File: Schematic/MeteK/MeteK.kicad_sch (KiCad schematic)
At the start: 6 parts, among them U1 Pico, U2 LM7805_TO220

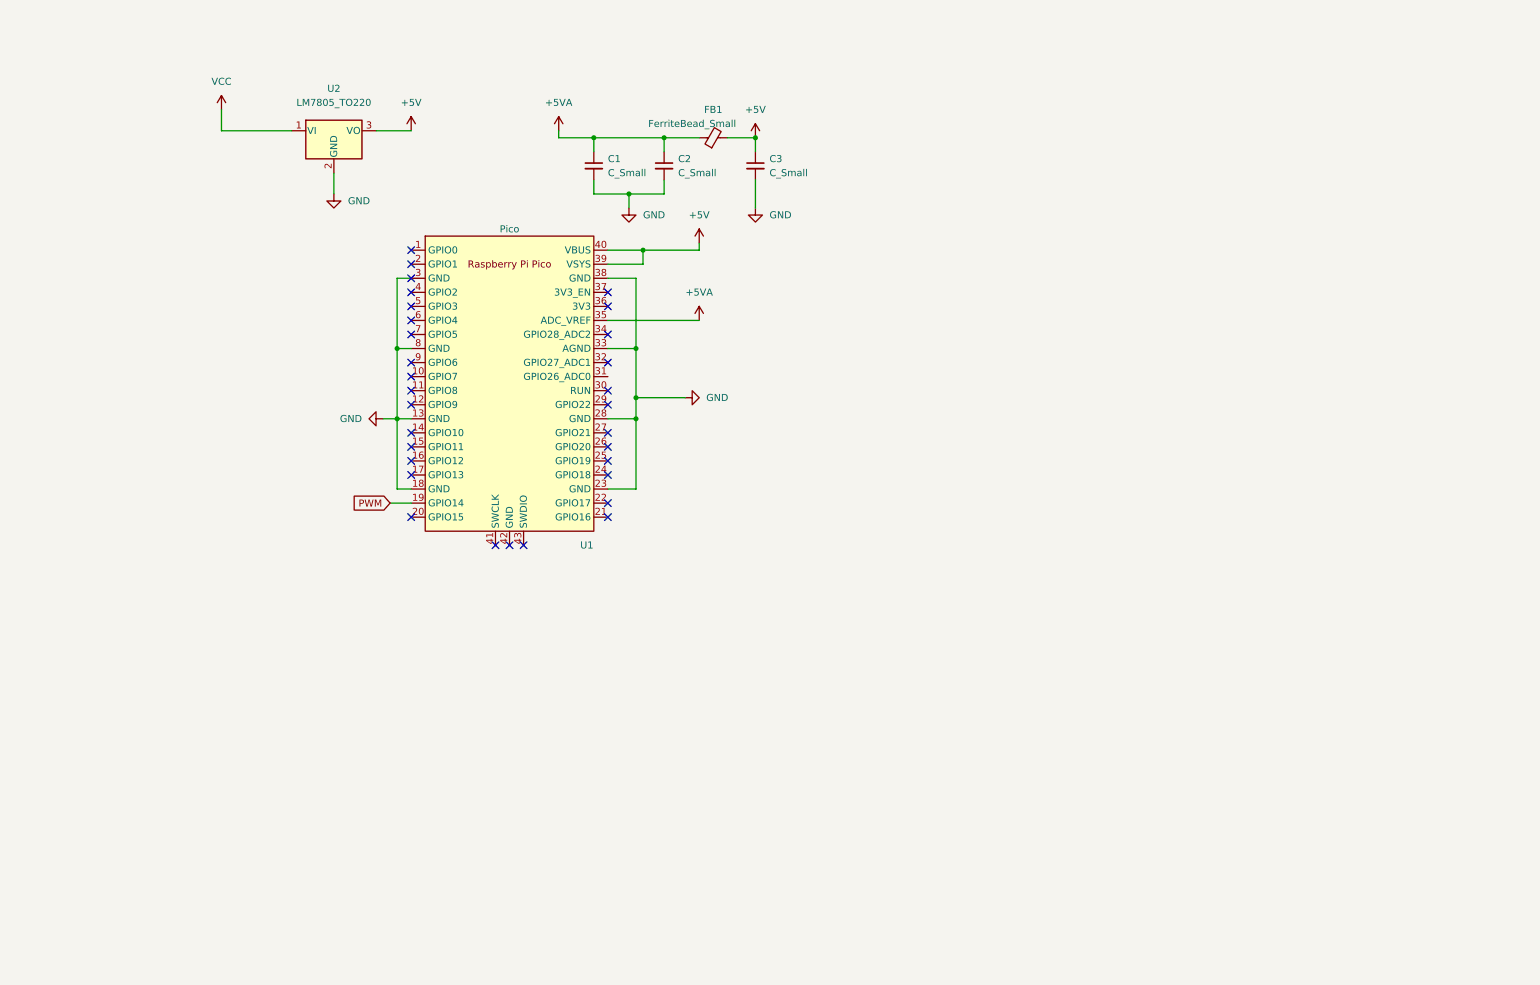
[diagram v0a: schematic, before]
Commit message: Gate driver fixes. Initial KiCad schematic and PCB design trials. Updates on components.
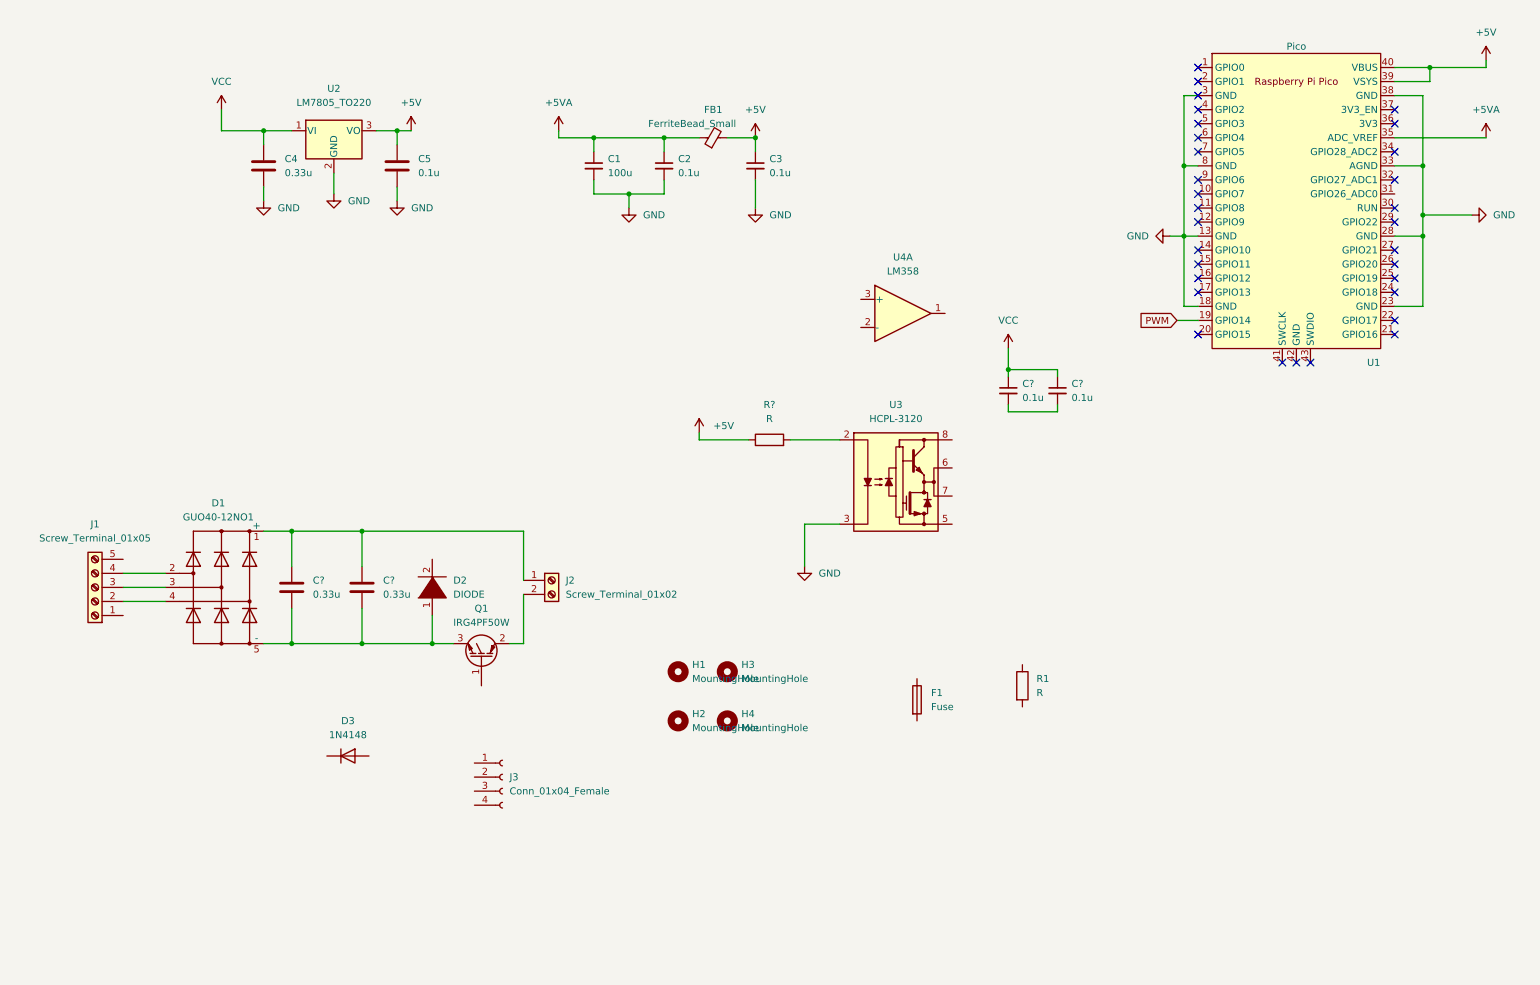
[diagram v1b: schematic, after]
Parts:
- added C4, C? (x2): 0.33u, Capacitor_THT:C_Disc_D3.4mm_W2.1mm_P2.50mm, symbol Device:C
- added C5: 0.1u, Capacitor_THT:C_Disc_D5.0mm_W2.5mm_P2.50mm, symbol Device:C
- added C? (x2): 0.1u, Capacitor_THT:C_Disc_D14.5mm_W5.0mm_P10.00mm, symbol Device:C_Small
- added D1: GUO40-12NO1, Diode_THT:Diode_Bridge_IXYS_GUFP, symbol Diode_Bridge:GUO40-12NO1
- added D2: DIODE, Package_TO_SOT_THT:TO-220-2_Horizontal_TabUp, symbol pspice:DIODE
- added D3: 1N4148, Diode_THT:D_DO-35_SOD27_P7.62mm_Horizontal, symbol Diode:1N4148
- added F1: Fuse, Fuse:Fuse_Bourns_MF-RG1100, symbol Device:Fuse
- added H1, H2, H3, H4: MountingHole, MountingHole:MountingHole_3.2mm_M3, symbol Mechanical:MountingHole
- added J1: Screw_Terminal_01x05, TerminalBlock_MetzConnect:TerminalBlock_MetzConnect_Type101_RT01605HBWC_1x05_P5.08mm_Horizontal, symbol Connector:Screw_Terminal_01x05
- added J2: Screw_Terminal_01x02, TerminalBlock_MetzConnect:TerminalBlock_MetzConnect_Type101_RT01602HBWC_1x02_P5.08mm_Horizontal, symbol Connector:Screw_Terminal_01x02
- added J3: Conn_01x04_Female, Connector:FanPinHeader_1x04_P2.54mm_Vertical, symbol Connector:Conn_01x04_Female
- added Q1: IRG4PF50W, Package_TO_SOT_THT:TO-247-3_Vertical, symbol Transistor_IGBT:IRG4PF50W
- added R1, R?: R, Resistor_THT:R_Axial_DIN0516_L15.5mm_D5.0mm_P7.62mm_Vertical, symbol Device:R
- added U3: HCPL-3120, Package_DIP:DIP-8_W7.62mm, symbol Driver_FET:HCPL-3120
- added U4: LM358, Package_DIP:DIP-8-16_W7.62mm, symbol Amplifier_Operational:LM358
- C1: value C_Small -> 100u; footprint (none) -> Capacitor_THT:C_Disc_D16.0mm_W5.0mm_P10.00mm
- C2: value C_Small -> 0.1u; footprint (none) -> Capacitor_THT:C_Disc_D14.5mm_W5.0mm_P10.00mm
- C3: value C_Small -> 0.1u; footprint (none) -> Capacitor_THT:C_Disc_D4.3mm_W1.9mm_P5.00mm
- FB1: footprint (none) -> Inductor_SMD:L_2512_6332Metric
- U1: footprint RPi_Pico:RPi_Pico_SMD_TH -> MCU_RaspberryPi_and_Boards:RPi_Pico_SMD_TH
- U2: footprint Package_TO_SOT_THT:TO-220-3_Vertical -> Package_TO_SOT_THT:TO-220-3_Horizontal_TabDown
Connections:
- net +5V: now also C5.1, R?.1
- net GND: now also C4.2, C5.2, U3.3 (C)
- net VCC: now also C4.1, C?.1, C?.1
- new net: C?.1, C?.1, D1.1 (+), J2.1 (Pin_1)
- new net: C?.2, C?.2, D1.5 (-), D2.1 (K), Q1.3 (E)
- new net: C?.2, C?.2
- new net: J2.2 (Pin_2), Q1.2 (C)
- new net: D1.4, J1.2 (Pin_2)
- new net: D1.3, J1.3 (Pin_3)
- new net: D1.2, J1.4 (Pin_4)
- new net: R?.2, U3.2 (A)
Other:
- moved on the sheet: U1

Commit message: further tests on schematic and pcb layout.
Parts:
- removed C3: 0.1u, Capacitor_THT:C_Disc_D4.3mm_W1.9mm_P5.00mm, symbol Device:C_Small
- removed C? (x2): 0.1u, Capacitor_THT:C_Disc_D14.5mm_W5.0mm_P10.00mm, symbol Device:C_Small
- removed FB1: FerriteBead_Small, Inductor_SMD:L_2512_6332Metric, symbol Device:FerriteBead_Small
- removed J3: Conn_01x04_Female, Connector:FanPinHeader_1x04_P2.54mm_Vertical, symbol Connector:Conn_01x04_Female
- removed R1: R, Resistor_THT:R_Axial_DIN0516_L15.5mm_D5.0mm_P7.62mm_Vertical, symbol Device:R
- removed U2: LM7805_TO220, Package_TO_SOT_THT:TO-220-3_Horizontal_TabDown, symbol Regulator_Linear:LM7805_TO220
- removed U4: LM358, Package_DIP:DIP-8-16_W7.62mm, symbol Amplifier_Operational:LM358
- added C10, C3: 0.33uF, Capacitor_SMD:C_1206_3216Metric, symbol Device:C
- added C11, C12: 0.1uF, Capacitor_SMD:C_1206_3216Metric, symbol Device:C
- added C13, C8: 0.01uF, Capacitor_SMD:C_1206_3216Metric, symbol Device:C_Small
- added C9: 0.1uF, Capacitor_SMD:C_1206_3216Metric, symbol Device:C_Small
- added J3: Conn_01x02_Female, Connector_PinHeader_2.54mm:PinHeader_1x02_P2.54mm_Vertical, symbol Connector:Conn_01x02_Female
- added J4: Conn_01x03_Female, Connector_PinHeader_2.54mm:PinHeader_1x03_P2.54mm_Vertical, symbol Connector:Conn_01x03_Female
- added L1: 27n, Inductor_SMD:L_1206_3216Metric, symbol Device:L_Small
- added R2, R3: 220R, Resistor_SMD:R_0805_2012Metric, symbol Device:R_Small
- added R4: 22R, Resistor_SMD:R_0805_2012Metric, symbol Device:R_Small
- added R5: 22kR, Resistor_SMD:R_0805_2012Metric, symbol Device:R_Small
- added R6: 39kR, Resistor_SMD:R_0805_2012Metric, symbol Device:R_Small
- added R7: 440, Resistor_SMD:R_0805_2012Metric, symbol Device:R_Small
- added U2: L78L33_SOT89, Package_TO_SOT_SMD:SOT-89-3, symbol Regulator_Linear:L78L33_SOT89
- added U4: L78L05_SOT89, Package_TO_SOT_SMD:SOT-89-3, symbol Regulator_Linear:L78L05_SOT89
- added U5: L78L12_SOT89, Package_TO_SOT_SMD:SOT-89-3, symbol Regulator_Linear:L78L12_SOT89
- added U6: LM358, Package_DIP:DIP-8_W7.62mm, symbol pspice:OPAMP
- C1: value 100u -> 1uF; footprint Capacitor_THT:C_Disc_D16.0mm_W5.0mm_P10.00mm -> Capacitor_SMD:C_1206_3216Metric
- C2: value 0.1u -> 0.1uF; footprint Capacitor_THT:C_Disc_D14.5mm_W5.0mm_P10.00mm -> Capacitor_SMD:C_1206_3216Metric
- C4: value 0.33u -> 0.33uF; footprint Capacitor_THT:C_Disc_D3.4mm_W2.1mm_P2.50mm -> Capacitor_SMD:C_1206_3216Metric
- C5: value 0.1u -> 0.1uF; footprint Capacitor_THT:C_Disc_D5.0mm_W2.5mm_P2.50mm -> Capacitor_SMD:C_1206_3216Metric
- C6, C7: renamed from C?; value 0.33u -> 470u; footprint Capacitor_THT:C_Disc_D3.4mm_W2.1mm_P2.50mm -> Capacitor_THT:CP_Radial_D35.0mm_P10.00mm_SnapIn
- D2: footprint Package_TO_SOT_THT:TO-220-2_Horizontal_TabUp -> Package_TO_SOT_THT:TO-220-2_Vertical
- D3: footprint Diode_THT:D_DO-35_SOD27_P7.62mm_Horizontal -> Diode_SMD:D_SMB
- F1: footprint Fuse:Fuse_Bourns_MF-RG1100 -> Fuse:Fuseholder_Clip-5x20mm_Bel_FC-203-22_Lateral_P17.80x5.00mm_D1.17mm_Horizontal
- H1, H2, H3, H4: footprint MountingHole:MountingHole_3.2mm_M3 -> MountingHole:MountingHole_3.2mm_M3_Pad
- R1: renamed from R?; value R -> 220; footprint Resistor_THT:R_Axial_DIN0516_L15.5mm_D5.0mm_P7.62mm_Vertical -> Resistor_SMD:R_0603_1608Metric
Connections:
- net +5V: now also C12.1, J4.1 (Pin_1), U4.1 (OUT); no longer C5.1, R1.1, U1.39 (VSYS), U1.40 (VBUS)
- net GND: now also J1.5 (Pin_5), C10.2, C11.2, C12.2, C13.2, C3.2, J3.1 (Pin_1), J4.3 (Pin_3), R6.2, U2.2 (GND), U4.2 (GND), U5.2 (GND), U6.5 (V-)
- net PWM: now also R1.1, U1.1 (GPIO0); no longer U1.19 (GPIO14)
- net VCC: now also J1.4 (Pin_4), U3.8 (VCC), C10.1, C13.1, C3.1, C8.1, C9.1, U2.3 (IN), U4.3 (IN), U5.3 (IN), U6.4 (V+)
- net A+: now reaches C6.1, C7.1
- net A+: now also D2.2 (A), F1.2, J2.2 (Pin_2); no longer D1.1 (+), J2.1 (Pin_1)
- net REC_-: now reaches C6.2, C7.2, D1.5 (-), Q1.3 (E)
- net REC_-: now also U3.5 (VEE), C8.2, C9.2, R4.2; no longer D2.1 (K)
- net A-: now reaches Q1.2 (C)
- net A-: now also D2.1 (K), J2.1 (Pin_1); no longer J2.2 (Pin_2)
- net at U1.31 (GPIO26_ADC0): now also R7.1
- net GATE: now reaches Q1.1 (G)
- net GATE: now also R2.2, R3.2, R4.1
- net AC_c: now reaches J1.1 (Pin_1)
- net AC_c: now also D1.2
- net AC_a: now reaches D1.4
- net AC_a: now also J1.3 (Pin_3); no longer J1.2 (Pin_2)
- net AC_b: now reaches D1.3
- net AC_b: now also J1.2 (Pin_2); no longer J1.3 (Pin_3)
- net at D3.1 (K): now also U3.6 (VO), U3.7 (VO), R2.1
- net at D3.2 (A): now also R3.1
- net at F1.1: now also D1.1 (+)
- net +5VA renamed +3.3VA
- net +3.3VA: now also L1.1
- new net: R5.2, R6.1, U6.1 (+)
- new net +12V: C11.1, J3.2 (Pin_2), U5.1 (OUT)
- new net +3.3V: C5.1, L1.2, U1.39 (VSYS), U2.1 (OUT)
- new net CSENSE: J4.2 (Pin_2), R5.1
- new net C_ADC: R7.2, U6.2 (-), U6.3
- no-connect marks 31 -> 32
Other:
- moved on the sheet: C1, C2, C4, C5, C6, C7, D1, D2, D3, F1, H1, H2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
